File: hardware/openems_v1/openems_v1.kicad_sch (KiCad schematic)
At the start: 0 parts

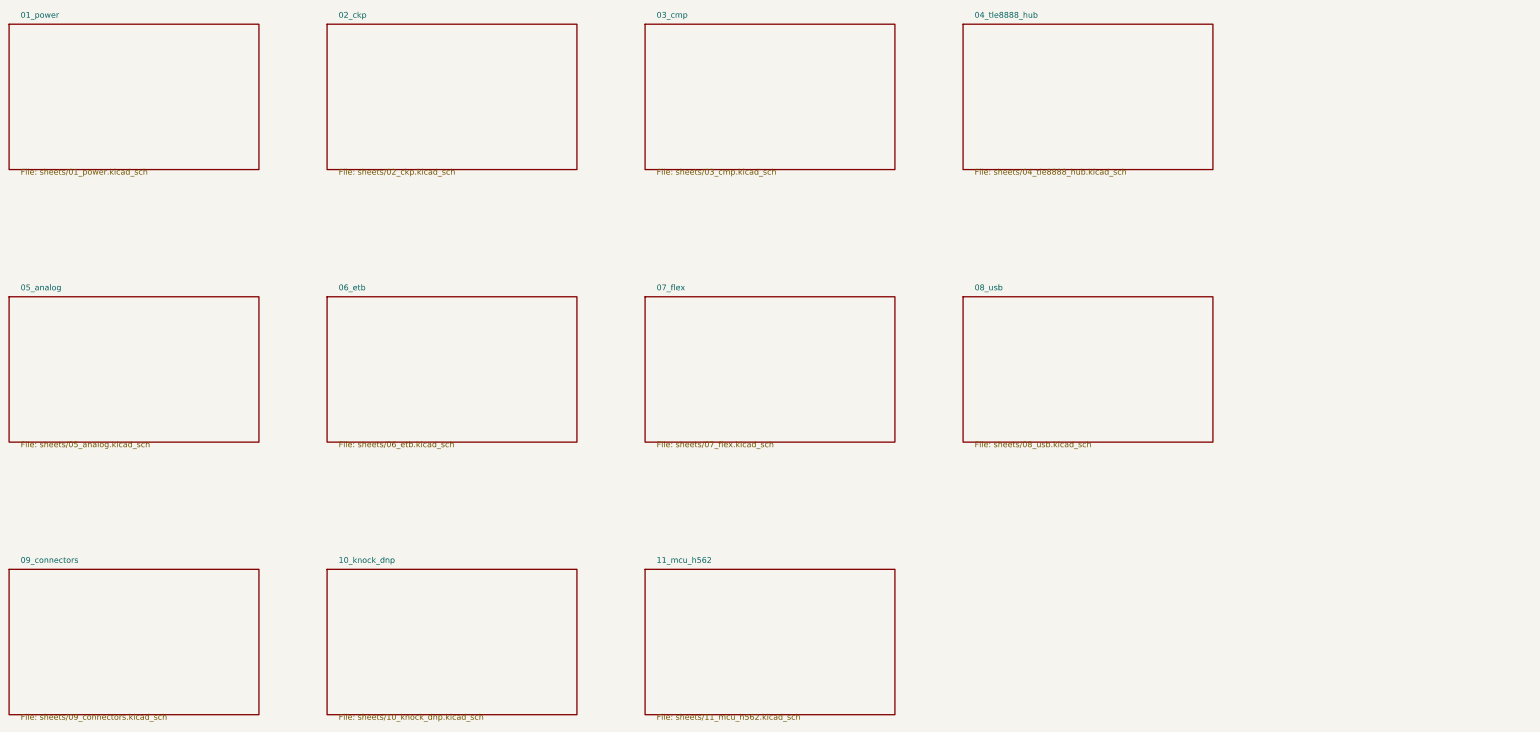
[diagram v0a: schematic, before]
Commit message: feat(hw): passo 6 — hierarquia root v2, TLE8888 hub/ETB substituídos por 04a-d
- 04_tle8888_hub e 06_etb (ambas vazias, zero cobre) removidas da hierarquia
- 4 sheets novas ligadas no lugar: 04_pmic_tps65381 (TPS65381A-Q1),
  04_drive_mc33810 (INJ/IGN), 04_bridge_l9960t (ETB+EWG, substitui 06_etb),
  04_wbo2_cj125 (CJ125) — cada uma só com título, conteúdo fica p/ quando os
  símbolos dos CIs existirem
- root openems_v1.kicad_sch A4→A3: com 13 sheets os boxes por defeito
  (80x50) não cabiam no grid 55x32 sem sobrepor umas às outras nem o cartão
  de título — corrigido antes de commitar (render conferido)
- add_hierarchical_sheet recalculou os instance-paths dos componentes nas
  restantes sheets (03_cmp/05_analog/07_flex/11_mcu_h562) — mudança
  esperada da ferramenta, não edição manual

ERC do projecto: 64 erros / 129 avisos, inalterado face à baseline anterior
ao passo 6 (sheets 04*/06/08/09/10 continuam vazias — não é regressão).

Co-Authored-By: Claude Sonnet 5 <noreply@anthropic.com>
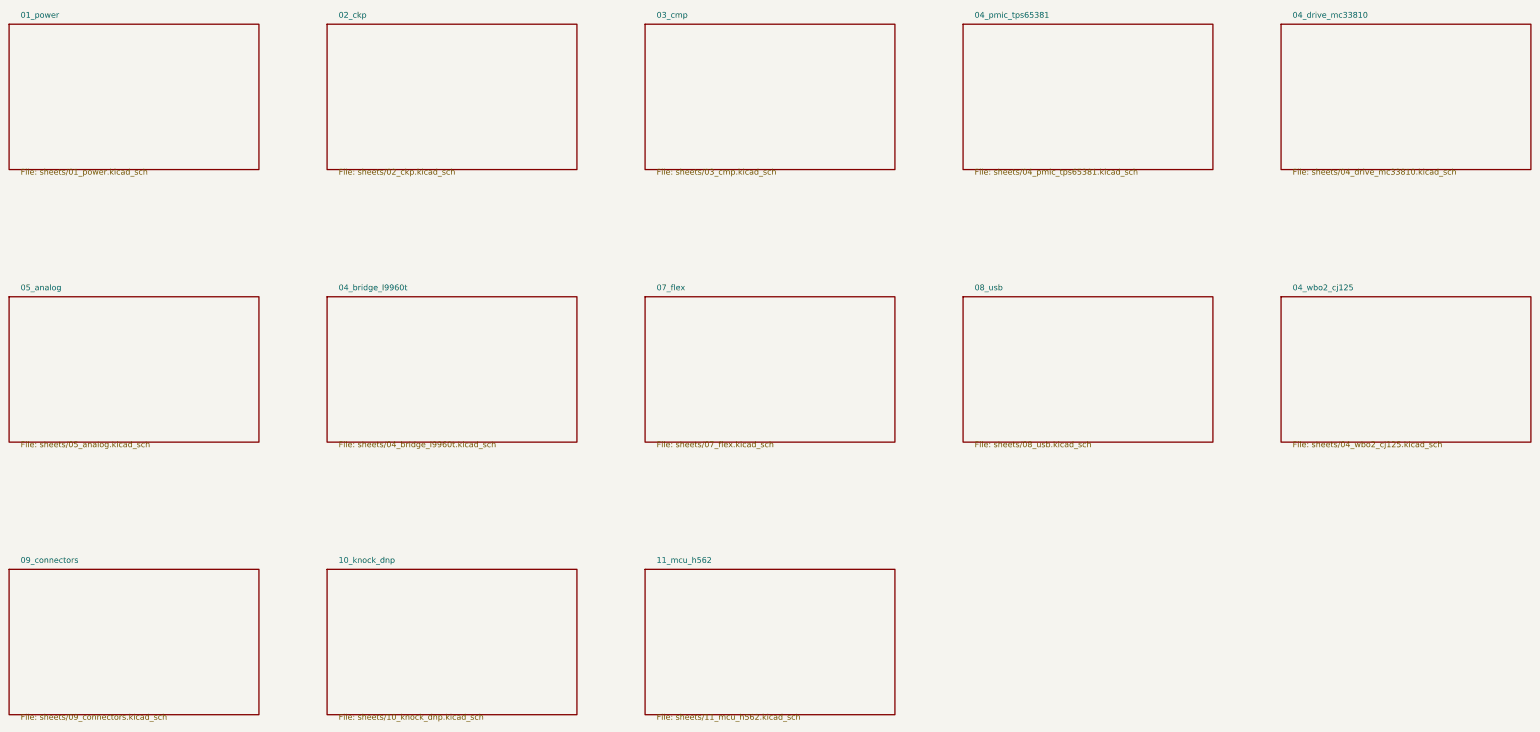
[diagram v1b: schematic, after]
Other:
- removed sheet 04_tle8888_hub
- removed sheet 06_etb
- added sheet 04_bridge_l9960t (sheets/04_bridge_l9960t.kicad_sch)
- added sheet 04_drive_mc33810 (sheets/04_drive_mc33810.kicad_sch)
- added sheet 04_pmic_tps65381 (sheets/04_pmic_tps65381.kicad_sch)
- added sheet 04_wbo2_cj125 (sheets/04_wbo2_cj125.kicad_sch)
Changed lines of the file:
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@@
 (kicad_sch (version 20260101) (generator "eeschema") (generator_version "10.0")
-  (paper "A4")
+  (paper "A3")
   (sheet (at 20.0 30.0) (size 55.0 32.0) (fields_autoplaced yes)
     (stroke (width 0.0006) (type default))
@@
     )
   )
-  (sheet (at 230.0 30.0) (size 55.0 32.0) (fields_autoplaced yes)
-    (stroke (width 0.0006) (type default))
-    (fill (color 0 0 0 0.0000))
-    (property "Sheet name" "04_tle8888_hub" (at 232.54 28.73 0)
-      (effects (font (size 1.27 1.27)) (justify left bottom))
-    )
-    (property "Sheet file" "sheets/04_tle8888_hub.kicad_sch" (at 232.54 63.27 0)
-      (effects (font (size 1.27 1.27)) (justify left bottom))
-    )
-  )
   (sheet (at 20.0 90.0) (size 55.0 32.0) (fields_autoplaced yes)
     (stroke (width 0.0006) (type default))
@@
     )
     (property "Sheet file" "sheets/05_analog.kicad_sch" (at 22.54 123.27 0)
-      (effects (font (size 1.27 1.27)) (justify left bottom))
-    )
-  )
-  (sheet (at 90.0 90.0) (size 55.0 32.0) (fields_autoplaced yes)
-    (stroke (width 0.0006) (type default))
-    (fill (color 0 0 0 0.0000))
-    (property "Sheet name" "06_etb" (at 92.54 88.73 0)
-      (effects (font (size 1.27 1.27)) (justify left bottom))
-    )
-    (property "Sheet file" "sheets/06_etb.kicad_sch" (at 92.54 123.27 0)
       (effects (font (size 1.27 1.27)) (justify left bottom))
     )
@@
     )
   )
+  (sheet (at 230.0 30.0) (size 55.0 32.0) (fields_autoplaced yes)
+    (stroke (width 0.0006) (type default))
+    (fill (color 0 0 0 0.0000))
+    (property "Sheet name" "04_pmic_tps65381" (at 232.54 28.73 0)
+      (effects (font (size 1.27 1.27)) (justify left bottom))
+    )
+    (property "Sheet file" "sheets/04_pmic_tps65381.kicad_sch" (at 232.54 63.27 0)
+      (effects (font (size 1.27 1.27)) (justify left bottom))
+    )
+  )
+  (sheet (at 90.0 90.0) (size 55.0 32.0) (fields_autoplaced yes)
+    (stroke (width 0.0006) (type default))
+    (fill (color 0 0 0 0.0000))
+    (property "Sheet name" "04_bridge_l9960t" (at 92.54 88.73 0)
+      (effects (font (size 1.27 1.27)) (justify left bottom))
+    )
+    (property "Sheet file" "sheets/04_bridge_l9960t.kicad_sch" (at 92.54 123.27 0)
+      (effects (font (size 1.27 1.27)) (justify left bottom))
+    )
+  )
+  (sheet (at 300.0 30.0) (size 55.0 32.0) (fields_autoplaced yes)
+    (stroke (width 0.0006) (type default))
+    (fill (color 0 0 0 0.0000))
+    (property "Sheet name" "04_drive_mc33810" (at 302.54 28.73 0)
+      (effects (font (size 1.27 1.27)) (justify left bottom))
+    )
+    (property "Sheet file" "sheets/04_drive_mc33810.kicad_sch" (at 302.54 63.27 0)
+      (effects (font (size 1.27 1.27)) (justify left bottom))
+    )
+  )
+  (sheet (at 300.0 90.0) (size 55.0 32.0) (fields_autoplaced yes)
+    (stroke (width 0.0006) (type default))
+    (fill (color 0 0 0 0.0000))
+    (property "Sheet name" "04_wbo2_cj125" (at 302.54 88.73 0)
+      (effects (font (size 1.27 1.27)) (justify left bottom))
+    )
+    (property "Sheet file" "sheets/04_wbo2_cj125.kicad_sch" (at 302.54 123.27 0)
+      (effects (font (size 1.27 1.27)) (justify left bottom))
+    )
+  )
   (sheet_instances
     (path "/" (page "1"))
@@
       (path "/79296e4b-3ad2-414d-b607-9eaf9f8a1416/02eec014-9ac6-452b-8cba-46601d19a07e" (page "3"))
       (path "/79296e4b-3ad2-414d-b607-9eaf9f8a1416/375cbaa1-0dd9-4ee5-9d66-d62d2e8350be" (page "4"))
-      (path "/79296e4b-3ad2-414d-b607-9eaf9f8a1416/aad8b78b-3b08-4f92-9f4d-0b1ebfd27e26" (page "5"))
       (path "/79296e4b-3ad2-414d-b607-9eaf9f8a1416/faf8653a-d8c2-45dc-ba76-2a710d11f5d0" (page "6"))
-      (path "/79296e4b-3ad2-414d-b607-9eaf9f8a1416/10ff57bc-30cf-4c3d-89f0-699d94ddb380" (page "7"))
       (path "/79296e4b-3ad2-414d-b607-9eaf9f8a1416/9a2b7e29-675b-4446-bb03-2d1d0fb3a4a2" (page "8"))
       (path "/79296e4b-3ad2-414d-b607-9eaf9f8a1416/2df4badf-5e0d-4ffa-941a-c58932edaf23" (page "9"))
@@
       (path "/79296e4b-3ad2-414d-b607-9eaf9f8a1416/4dd26149-b902-47bb-87af-917bc49fcb39" (page "11"))
       (path "/79296e4b-3ad2-414d-b607-9eaf9f8a1416/d0f5c832-7c50-4abd-ae75-882bdd652d97" (page "12"))
+      (path "/79296e4b-3ad2-414d-b607-9eaf9f8a1416/c7b9938d-8792-4eab-b90a-0e08b4f6bb76" (page "13"))
+      (path "/79296e4b-3ad2-414d-b607-9eaf9f8a1416/884bcc28-435d-473a-ad39-001ebef4788d" (page "14"))
+      (path "/79296e4b-3ad2-414d-b607-9eaf9f8a1416/ba32fb00-f1b6-409d-8278-3ce81aafb3be" (page "15"))
+      (path "/79296e4b-3ad2-414d-b607-9eaf9f8a1416/44b381ee-b47f-44e4-983d-f9406b788ea9" (page "16"))
   )
 )
